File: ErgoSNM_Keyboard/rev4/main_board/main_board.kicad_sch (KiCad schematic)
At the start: 11 parts, among them J1 Conn_MouseSensor, J3 Conn_MouseSensor, J4 Conn_02x10_Odd_Even, J5 Conn_02x10_Odd_Even, SW2 RESET, SW3 RESET

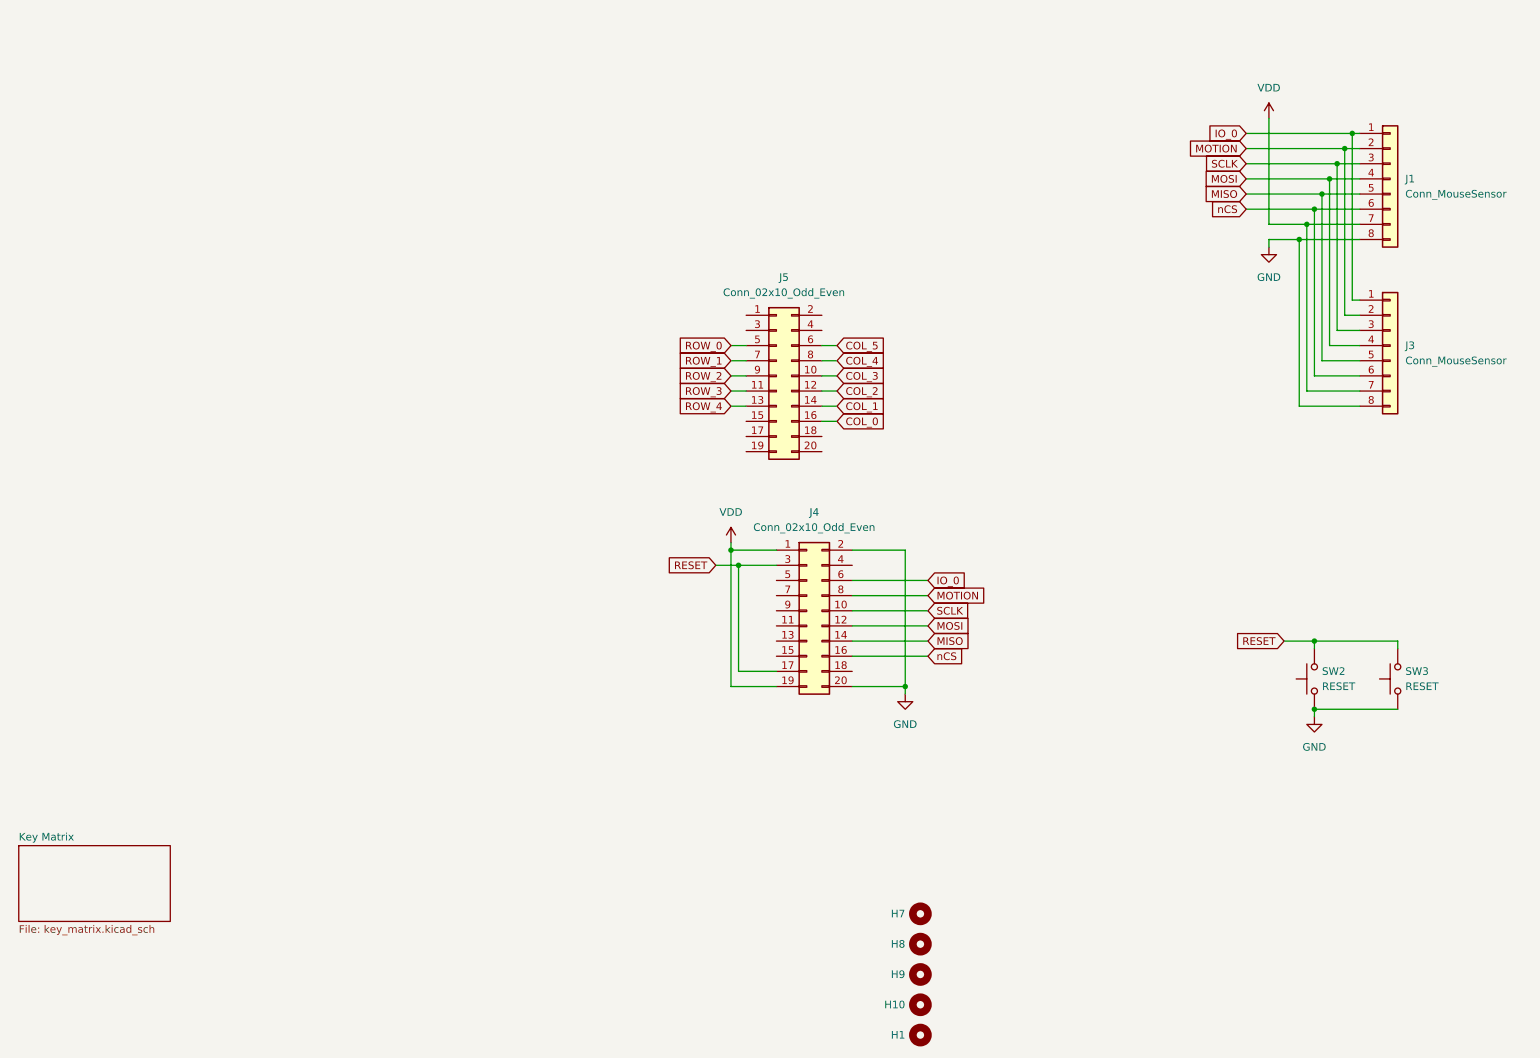
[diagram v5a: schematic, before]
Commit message: feat: update the connectors of the main board and core board
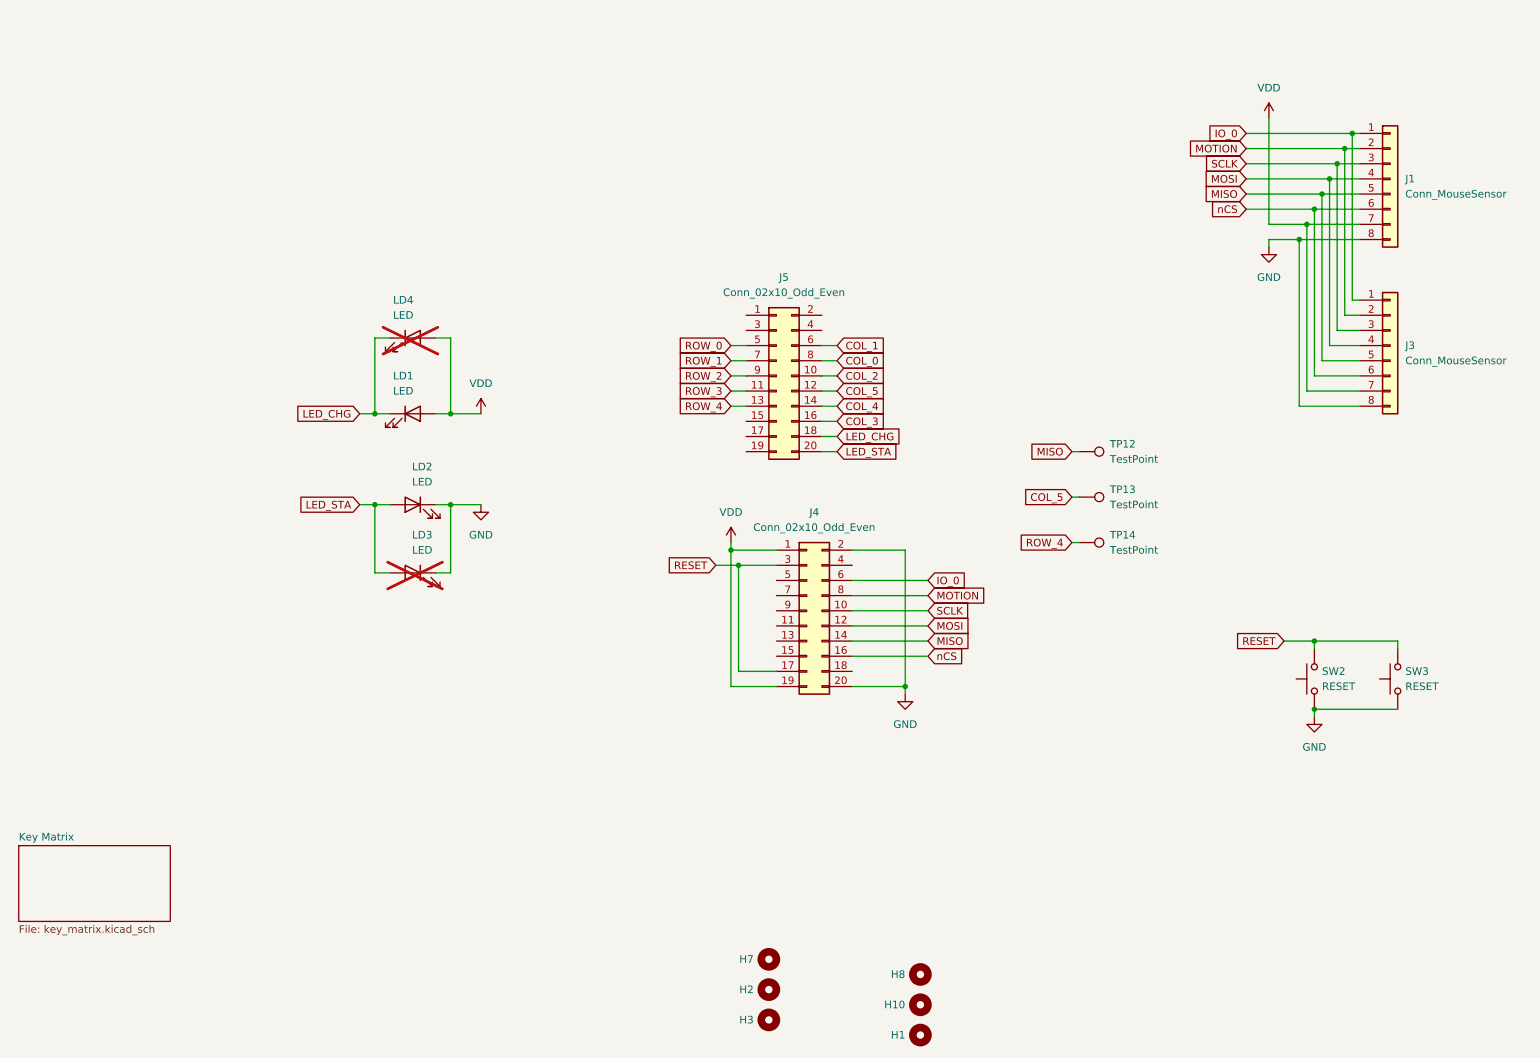
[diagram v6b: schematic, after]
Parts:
- removed H9: ~, MountingHole:MountingHole_2.7mm_M2.5_ISO14580, symbol Mechanical:MountingHole
- added H2, H3: ~, ErgoSNM_Keyboard:mounting_hole_6.5mm, symbol Mechanical:MountingHole
- added LD1, LD2, LD3, LD4: LED, LED_SMD:LED_0603_1608Metric_Pad1.05x0.95mm_HandSolder, symbol Device:LED
- added TP12, TP13, TP14: TestPoint, TestPoint:TestPoint_Pad_1.5x1.5mm, symbol Connector:TestPoint
- H7: footprint MountingHole:MountingHole_2.7mm_M2.5_ISO14580 -> ErgoSNM_Keyboard:mounting_hole_6.5mm
- J4, J5: now left out of the parts list
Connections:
- net COL_0: now also J5.8 (Pin_8); no longer J5.16 (Pin_16)
- net COL_1: now also J5.6 (Pin_6); no longer J5.14 (Pin_14)
- net COL_2: now also J5.10 (Pin_10); no longer J5.12 (Pin_12)
- net COL_3: now also J5.16 (Pin_16); no longer J5.10 (Pin_10)
- net COL_4: now also J5.14 (Pin_14); no longer J5.8 (Pin_8)
- net COL_5: now also J5.12 (Pin_12), TP13.1; no longer J5.6 (Pin_6)
- net GND: now also LD2.1 (K), LD3.1 (K)
- net MISO: now also TP12.1
- net ROW_4: now also TP14.1
- net VDD: now also LD1.2 (A), LD4.2 (A)
- net LED_CHG: now reaches J5.18 (Pin_18)
- net LED_CHG: now also LD1.1 (K), LD4.1 (K)
- net LED_STA: now reaches J5.20 (Pin_20)
- net LED_STA: now also LD2.2 (A), LD3.2 (A)
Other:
- moved on the sheet: H7, H8
